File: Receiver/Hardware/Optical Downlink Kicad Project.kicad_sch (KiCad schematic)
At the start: 18 parts, among them J1 Conn_01x20_Socket, J2 Conn_01x20_Socket, U1 OPA657U, U2 TLE2426-EP_D_8, U3 OPA657U, U4 ADS8691IPWR, U5 MEV3S0515SC, U6 HT7580-2

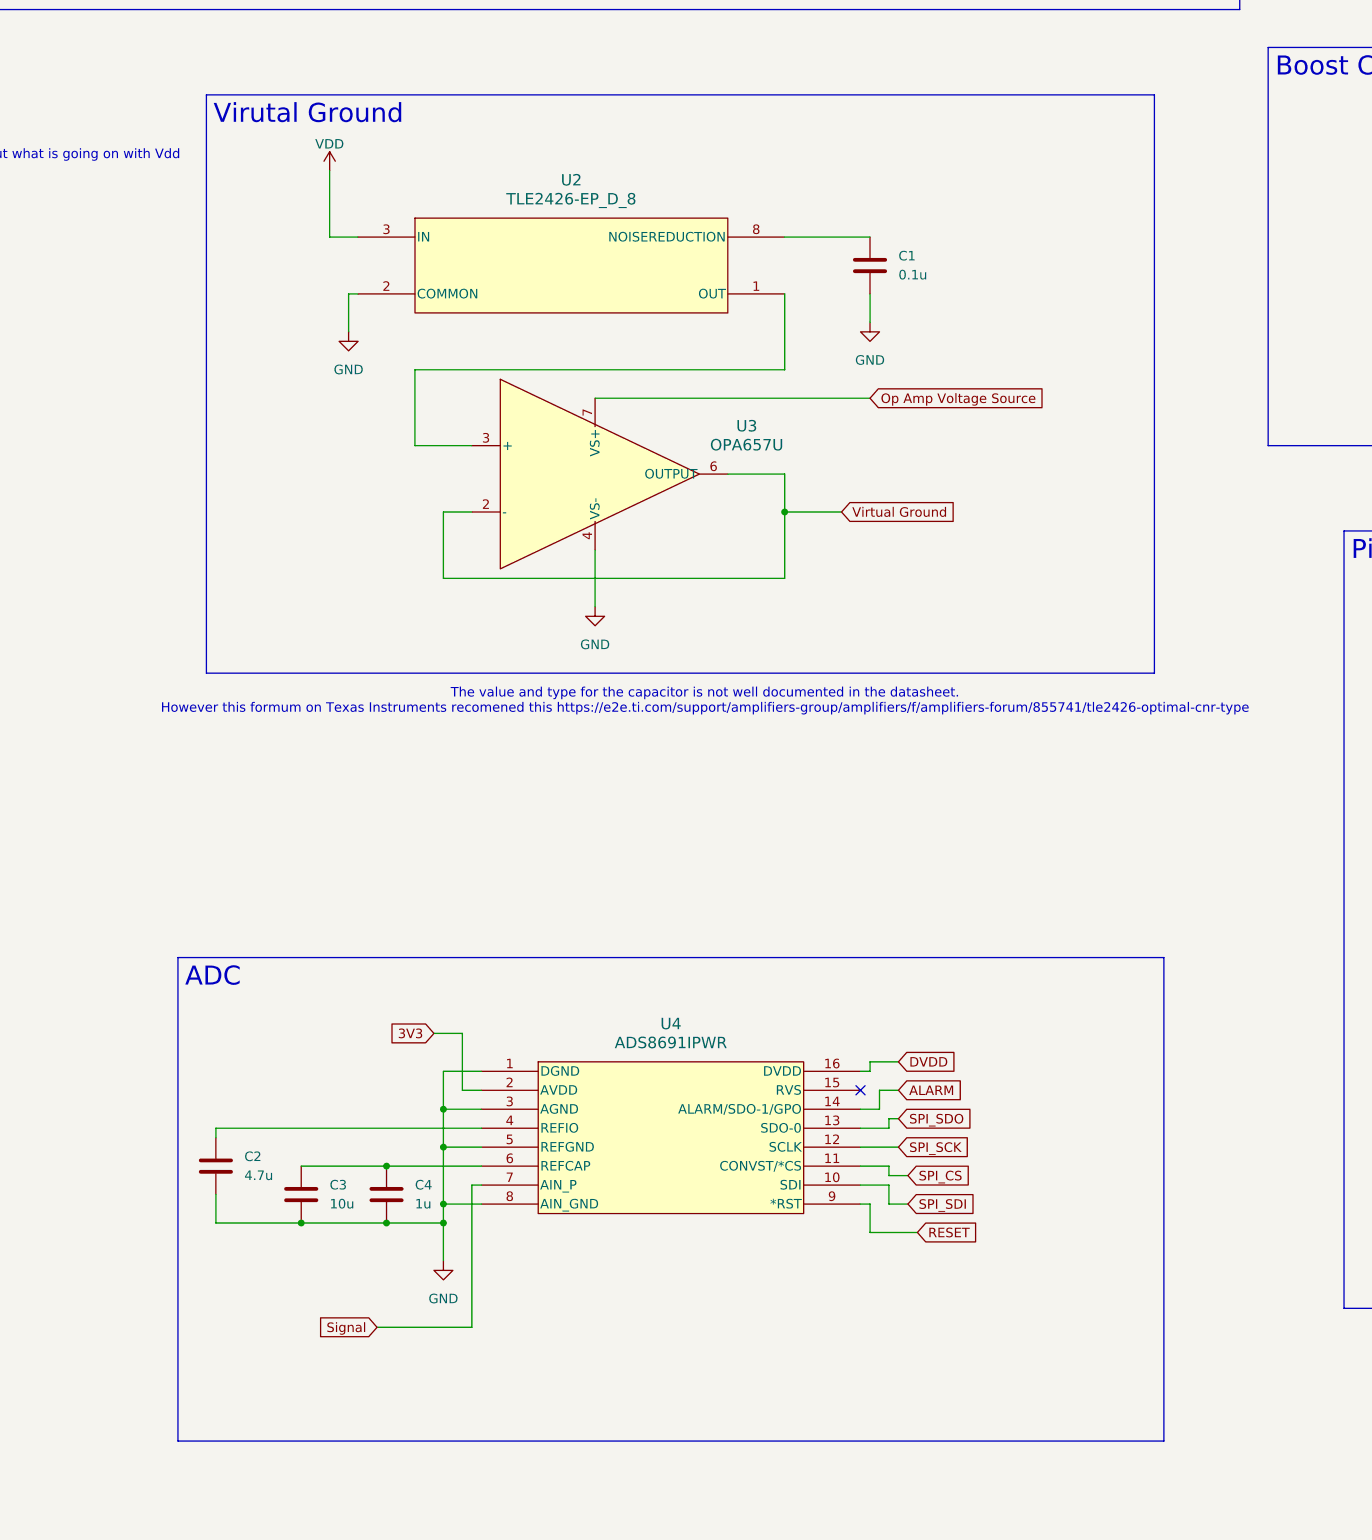
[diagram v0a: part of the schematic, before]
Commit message: Worked on Assigning Cap and R footprints
Also fixed an issue with some missing capacitors
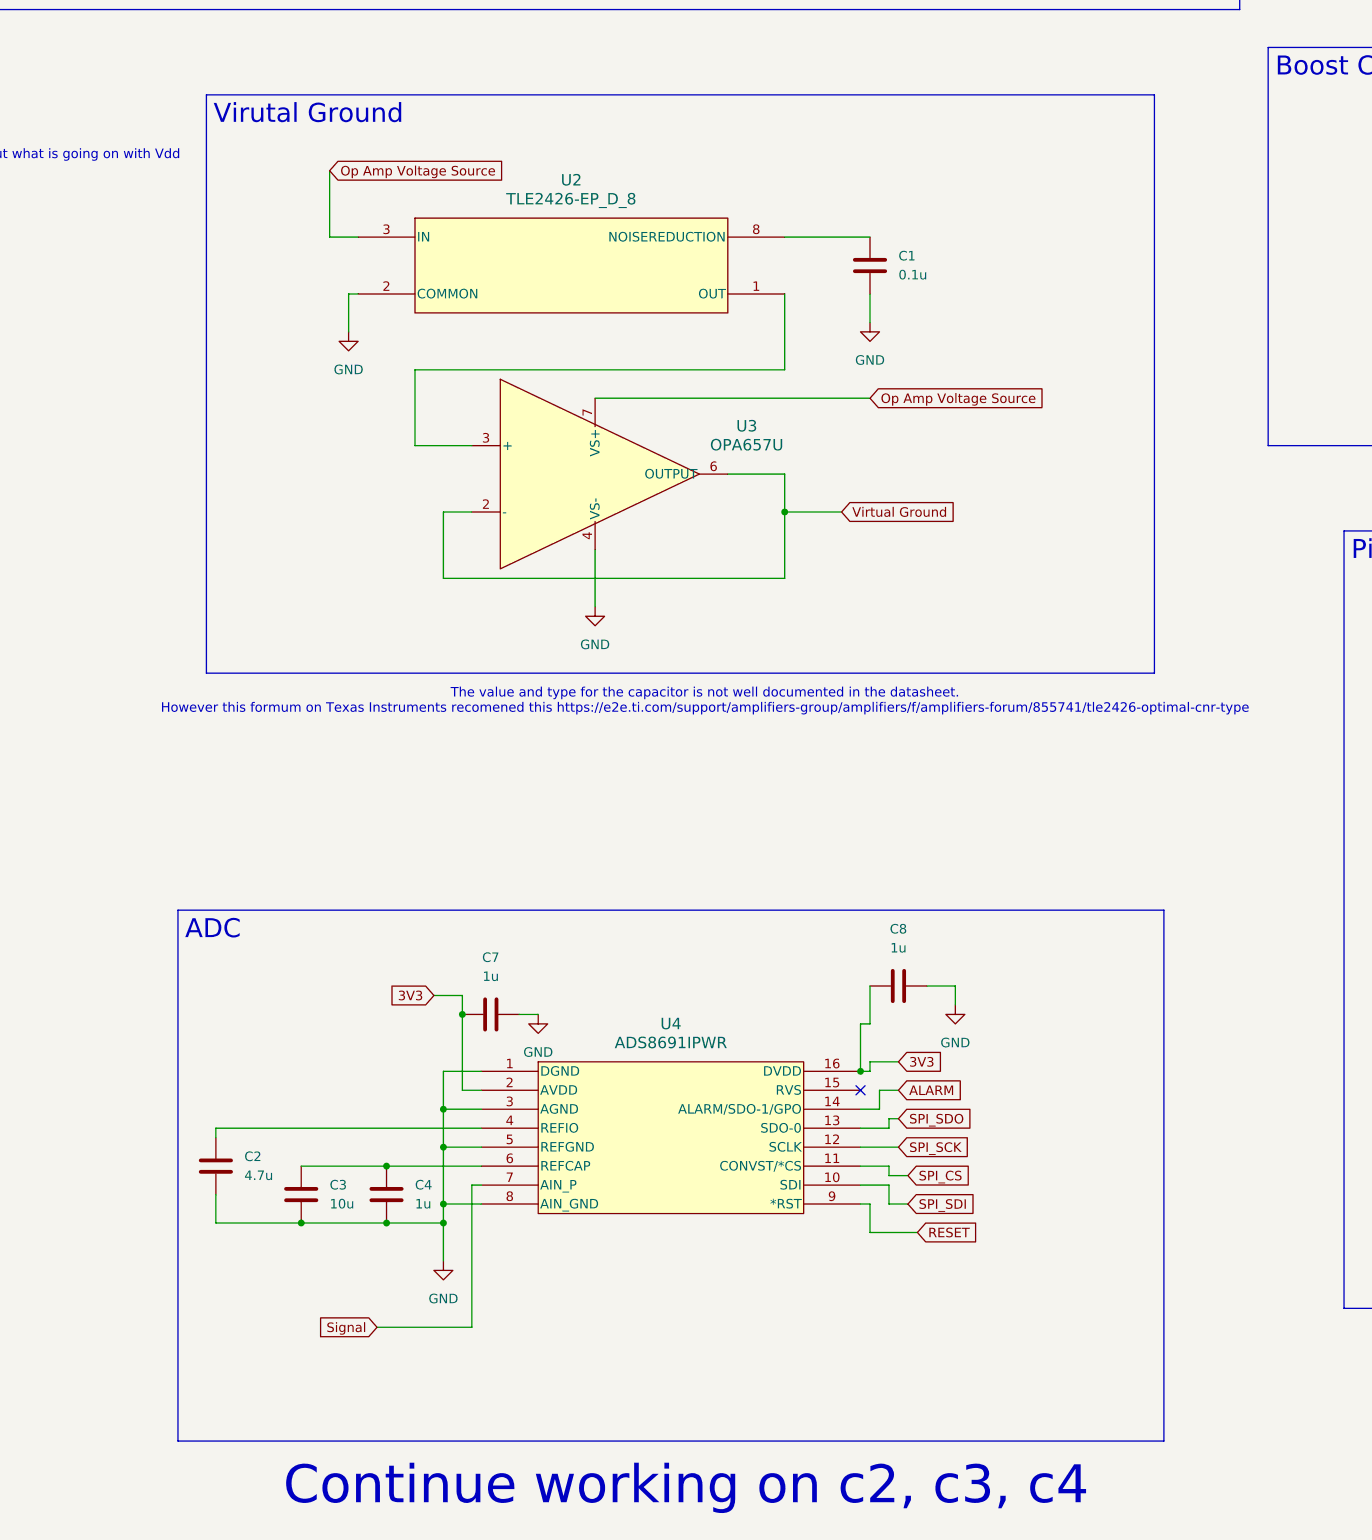
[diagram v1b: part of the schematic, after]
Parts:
- added C7, C8: 1u, 00-footprint-library:CAP_CL10_SAM, symbol Device:C
- C1: footprint Capacitor_SMD:CP_Elec_3x5.3 -> 00-footprint-library:CAPC1005X55N
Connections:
- net DVDD is gone; now on net 3V3: U4.16 (DVDD)
- net VDD is gone; now on net Op Amp Voltage Source: U2.3 (IN)
- net 3V3: now also C7.1, C8.1
- net GND: now also C7.2, C8.2
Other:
- note added: "Continue working on c2, c3, c4"

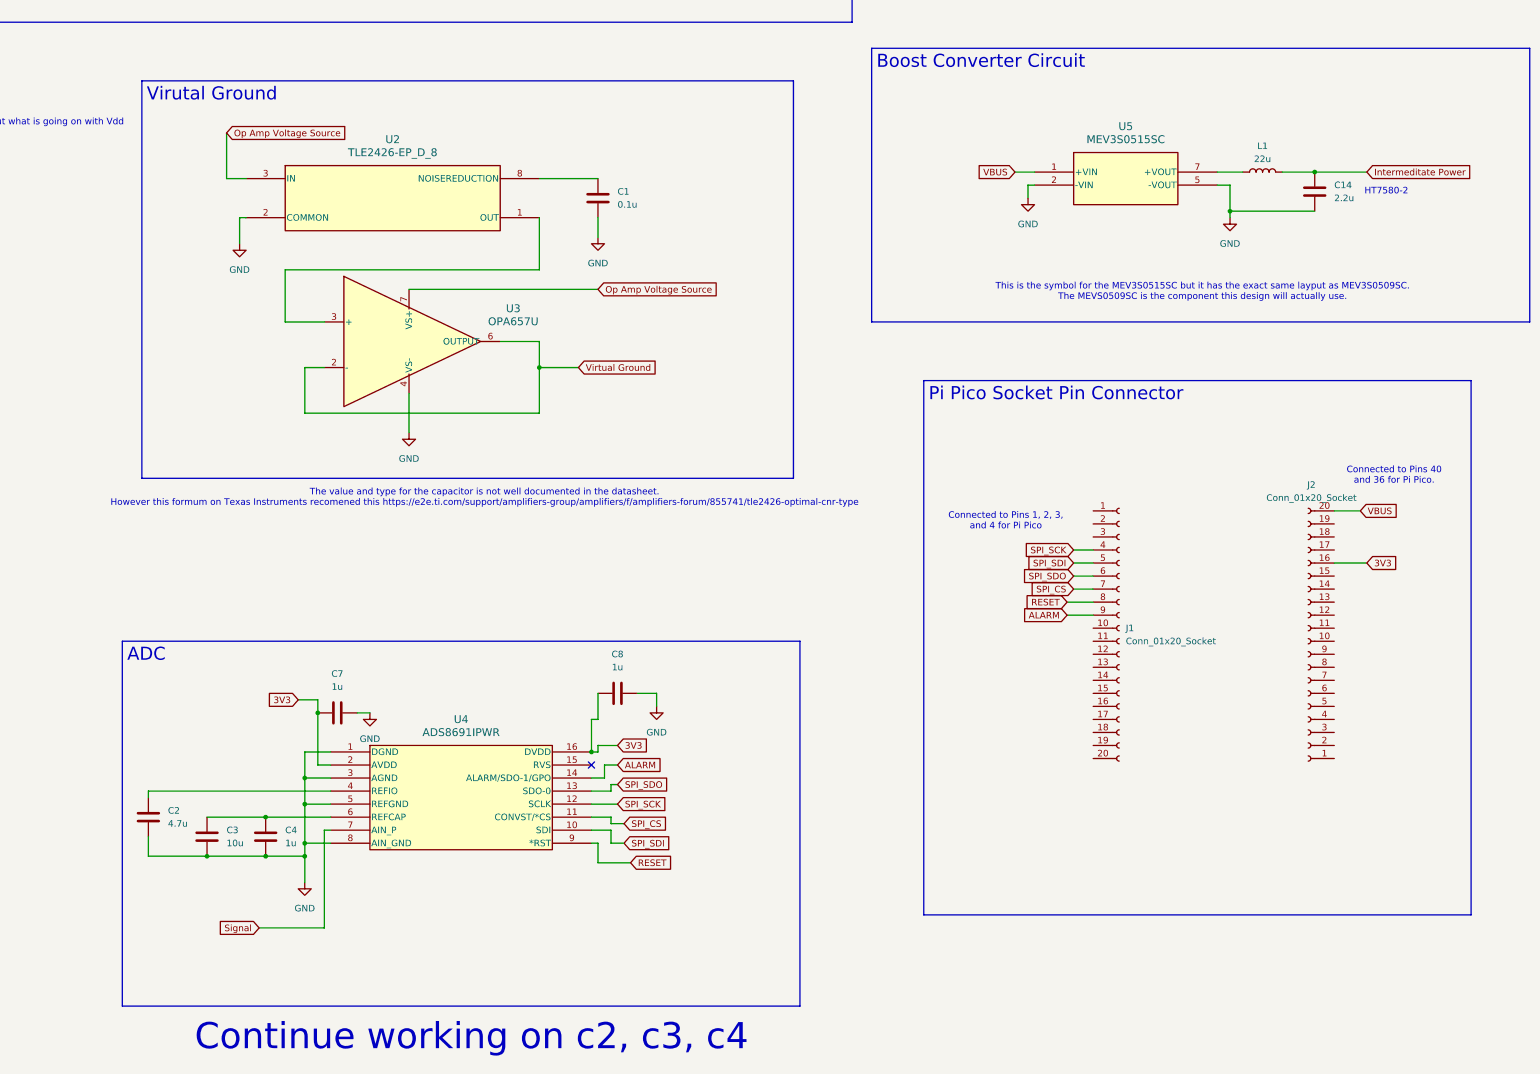
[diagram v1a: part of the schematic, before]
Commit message: Finished General Layout of PCB
Everything is pretty much finished for traces except gnd connections and clearing drc errors.
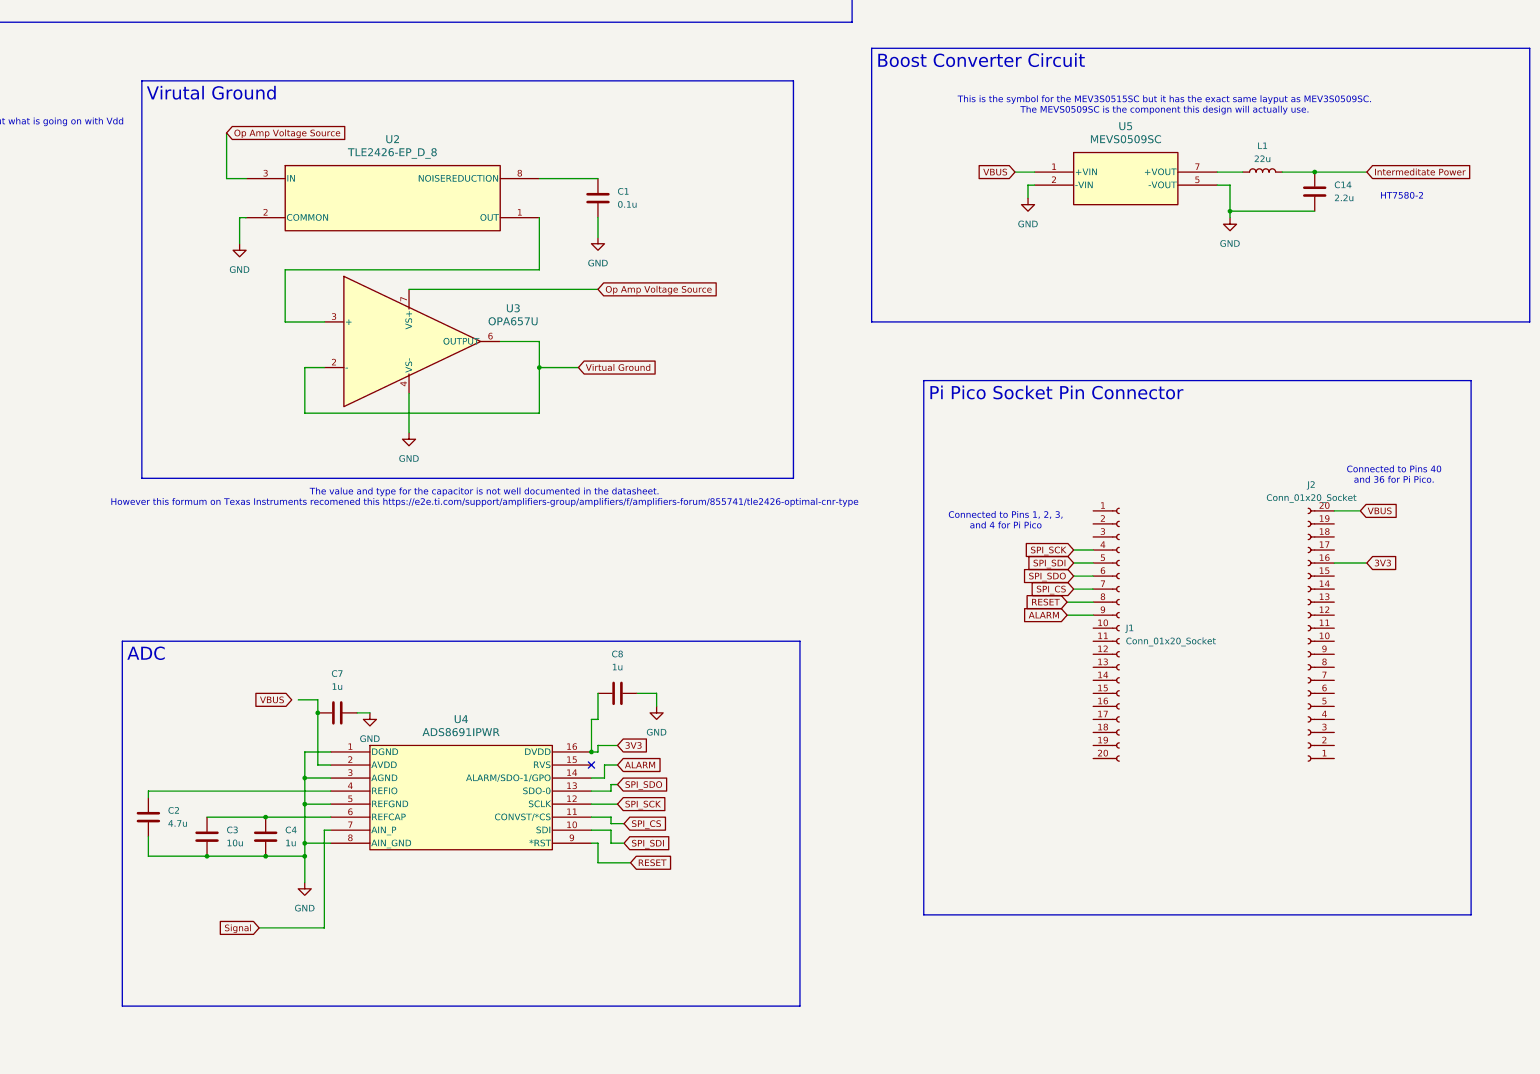
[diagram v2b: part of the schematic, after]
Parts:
- C14, C2: footprint Capacitor_SMD:CP_Elec_3x5.3 -> Capacitor_SMD:C_0603_1608Metric
- C3: footprint Capacitor_SMD:CP_Elec_3x5.3 -> Capacitor_SMD:C_0402_1005Metric
- C4: footprint Capacitor_SMD:CP_Elec_3x5.3 -> 00-footprint-library:CAP_CL10_SAM
- C5, C6: footprint Capacitor_Tantalum_SMD:CP_EIA-1608-08_AVX-J -> 00-footprint-library:CAPMP6.3X3.2_2.8N_KEM
- U5: value MEV3S0515SC -> MEVS0509SC
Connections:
- net 3V3: no longer C7.1, U4.2 (AVDD)
- new net: C7.1, U4.2 (AVDD)
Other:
- note removed: "Continue working on c2, c3, c4"
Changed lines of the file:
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@@
 	(text "HT7580-2"
 		(exclude_from_sim no)
-		(at 304.8 100.33 0)
+		(at 307.848 101.346 0)
 		(effects
 			(font
@@
 	(text "This is the symbol for the MEV3S0515SC but it has the exact same layput as MEV3S0509SC.\nThe MEVS0509SC is the component this design will actually use.\n"
 		(exclude_from_sim no)
-		(at 268.986 119.888 0)
+		(at 261.62 83.566 0)
 		(effects
 			(font
 				(size 1.27 1.27)
-			)
-		)
-	)
-	(text "Continue working on c2, c3, c4"
-		(exclude_from_sim no)
-		(at 126.492 265.176 0)
-		(effects
-			(font
-				(size 5.08 5.08)
+				(color 255 33 27 1)
 			)
 		)
@@
 		)
 	)
+	(global_label "VBUS"
+		(shape input)
+		(at 91.44 199.39 180)
+		(fields_autoplaced yes)
+		(effects
+			(font
+				(size 1.27 1.27)
+			)
+			(justify right)
+		)
+		(property "Intersheetrefs" "${INTERSHEET_REFS}"
+			(at 83.5562 199.39 0)
+			(effects
+				(font
+					(size 1.27 1.27)
+				)
+				(justify right)
+				(hide yes)
+			)
+		)
+	)
 	(global_label "Signal"
 		(shape output)
@@
 		)
 	)
-	(global_label "3V3"
-		(shape input)
-		(at 92.71 199.39 180)
-		(fields_autoplaced yes)
-		(effects
-			(font
-				(size 1.27 1.27)
-			)
-			(justify right)
-		)
-		(property "Intersheetrefs" "${INTERSHEET_REFS}"
-			(at 86.2172 199.39 0)
-			(effects
-				(font
-					(size 1.27 1.27)
-				)
-				(justify right)
-				(hide yes)
-			)
-		)
-	)
 	(global_label "SPI_SCK"
 		(shape input)
@@
 			)
 		)
-		(property "Datasheet" "~"
+		(property "Datasheet" "https://pip-assets.raspberrypi.com/categories/610-raspberry-pi-pico/documents/RP-008307-DS-1-pico-datasheet.pdf?disposition=inline"
 			(at 252.73 185.42 0)
 			(effects
@@
 			)
 		)
-		(property "Footprint" "Capacitor_Tantalum_SMD:CP_EIA-1608-08_AVX-J"
+		(property "Footprint" "00-footprint-library:CAPMP6.3X3.2_2.8N_KEM"
 			(at 275.2852 49.53 0)
 			(effects
@@
 			)
 		)
-		(property "Datasheet" "~"
+		(property "Datasheet" "https://yageogroup.com/content/datasheet/asset/file/KEM_T2005_T491"
 			(at 274.32 45.72 0)
 			(effects
@@
 			)
 		)
-		(property "Footprint" "Capacitor_SMD:CP_Elec_3x5.3"
+		(property "Footprint" "00-footprint-library:CAP_CL10_SAM"
 			(at 87.3252 229.87 0)
 			(effects
@@
 			)
 		)
-		(property "Datasheet" "~"
+		(property "Datasheet" "https://mm.digikey.com/Volume0/opasdata/d220001/medias/docus/3644/CL10B105KA8NNNC_spec.pdf"
 			(at 86.36 226.06 0)
 			(effects
@@
 			)
 		)
-		(property "Footprint" "Capacitor_SMD:CP_Elec_3x5.3"
+		(property "Footprint" "Capacitor_SMD:C_0603_1608Metric"
 			(at 64.4652 226.06 0)
 			(effects
@@
 			)
 		)
-		(property "Datasheet" "~"
+		(property "Datasheet" "https://mm.digikey.com/Volume0/opasdata/d220001/medias/docus/609/CL10A475KP8NNNC_Spec.pdf"
 			(at 63.5 222.25 0)
 			(effects
@@
 			)
 		)
-		(property "Datasheet" ""
+		(property "Datasheet" "https://datasheet4u.com/pdf-down/H/T/7/HT75xx-2_HoltekSemiconductor.pdf"
 			(at 260.35 40.64 0)
 			(effects
@@
 			)
 		)
-		(property "Footprint" "Capacitor_Tantalum_SMD:CP_EIA-1608-08_AVX-J"
+		(property "Footprint" "00-footprint-library:CAPMP6.3X3.2_2.8N_KEM"
 			(at 249.8852 49.53 0)
 			(effects
@@
 			)
 		)
-		(property "Datasheet" "~"
+		(property "Datasheet" "https://yageogroup.com/content/datasheet/asset/file/KEM_T2005_T491"
 			(at 248.92 45.72 0)
 			(effects
@@
 			)
 		)
-		(property "Footprint" "Capacitor_SMD:CP_Elec_3x5.3"
+		(property "Footprint" "Capacitor_SMD:C_0402_1005Metric"
 			(at 75.8952 229.87 0)
 			(effects
@@
 			)
 		)
-		(property "Datasheet" "~"
+		(property "Datasheet" "https://mm.digikey.com/Volume0/opasdata/d220001/medias/docus/2614/CL05A106MP5NUNC_Spec.pdf"
 			(at 74.93 226.06 0)
 			(effects
@@
 			)
 		)
-		(property "Footprint" "Capacitor_SMD:CP_Elec_3x5.3"
+		(property "Footprint" "Capacitor_SMD:C_0603_1608Metric"
 			(at 291.7952 104.14 0)
 			(effects
@@
 			)
 		)
-		(property "Datasheet" "~"
+		(property "Datasheet" "https://mm.digikey.com/Volume0/opasdata/d220001/medias/docus/4819/TMK107ABJ225KA-T_SS.pdf"
 			(at 290.83 100.33 0)
 			(effects
@@
 			)
 		)
-		(property "Value" "MEV3S0515SC"
+		(property "Value" "MEVS0509SC"
 			(at 254 90.17 0)
 			(effects
@@
 			)
 		)
-		(property "Datasheet" "MEV3S0515SC"
+		(property "Datasheet" "https://pim.murata.com/asset/pim4/isolatedDCDCconverter/KDC_MEV3_PDF_ISOLATEDDCDCCONVERTER?lastModifiedDatetime=20250707193634"
 			(at 257.048 81.534 0)
 			(effects
